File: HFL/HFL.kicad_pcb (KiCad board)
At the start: 2 copper layers, 62.6 x 37.6 mm, 26 parts, among them J1 FAULTS, J2 PWR, J3 HFR, J4 SHTDN, K1 G5V-1, K2 G5V-1, K3 G5V-1, K4 G5V-1, K5 G5V-2

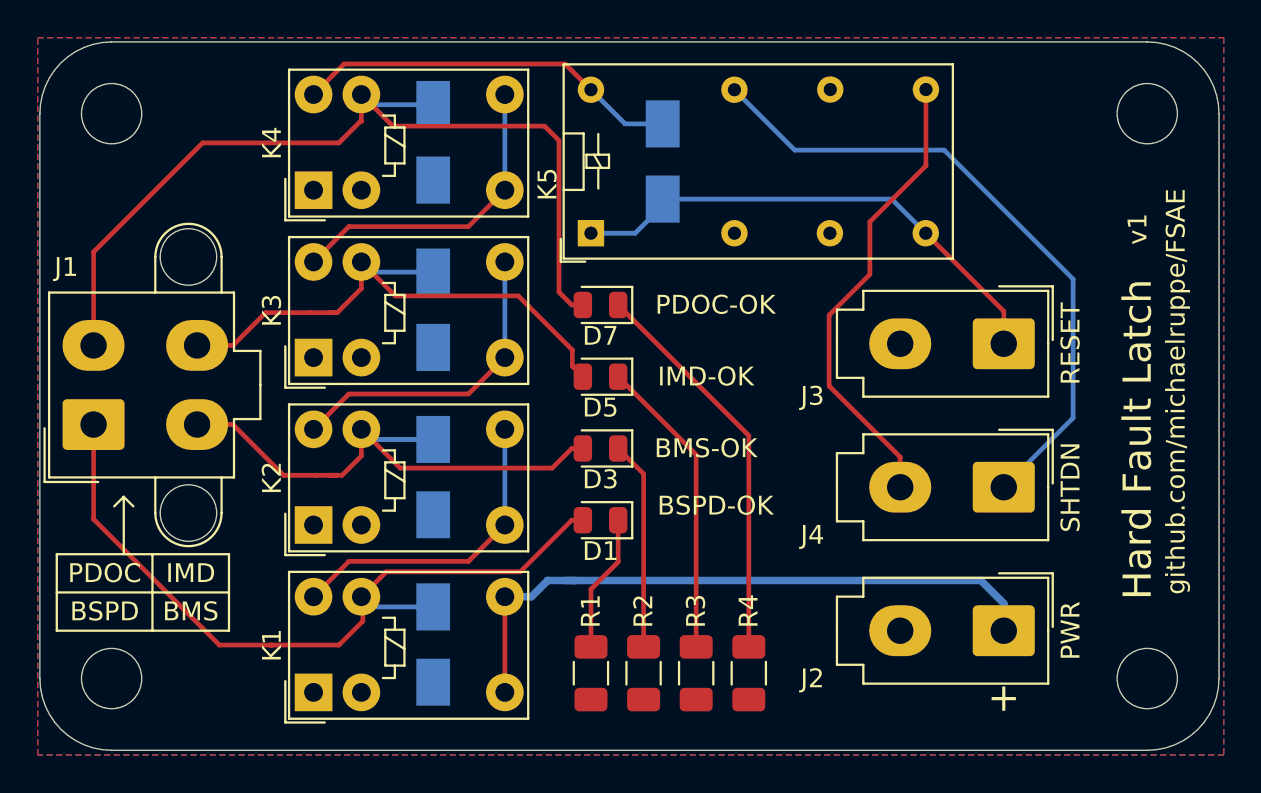
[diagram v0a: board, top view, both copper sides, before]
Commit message: Update HFL - include indicator lamp outputs (low-side)
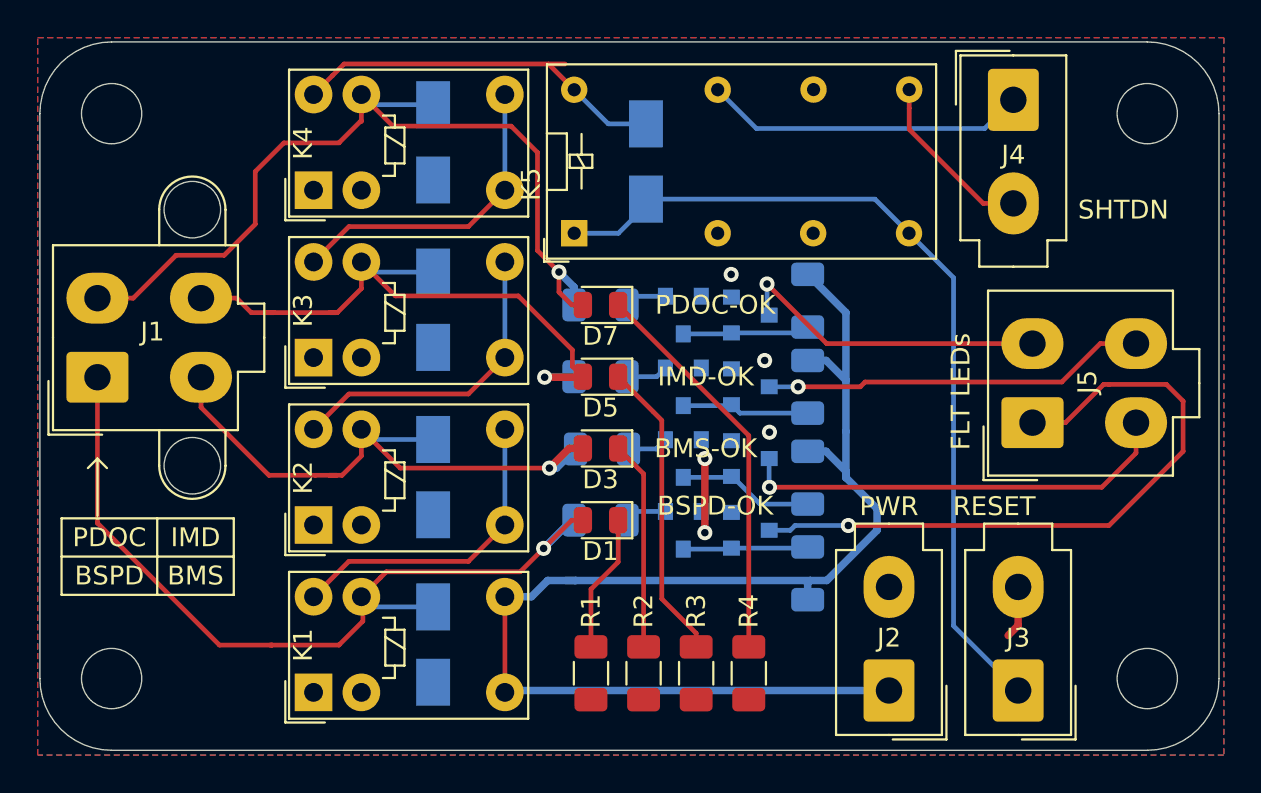
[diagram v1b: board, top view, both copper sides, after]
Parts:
- added J5: FLT-LT, Connector_Molex:Molex_Mini-Fit_Jr_5566-04A_2x02_P4.20mm_Vertical, F.Cu at (128.9, 65.9)
- added Q1: MMBT3904, Package_TO_SOT_SMD:SOT-23, B.Cu at (110.4, 67.8)
- added Q2: MMBT3904, Package_TO_SOT_SMD:SOT-23, B.Cu at (110.4, 60.2)
- added Q3: MMBT3904, Package_TO_SOT_SMD:SOT-23, B.Cu at (113.9, 67.8)
- added Q4: MMBT3904, Package_TO_SOT_SMD:SOT-23, B.Cu at (113.9, 60.2)
- added Q5: MMBT3904, Package_TO_SOT_SMD:SOT-23, B.Cu at (110.4, 64.0)
- added Q6: MMBT3904, Package_TO_SOT_SMD:SOT-23, B.Cu at (110.4, 71.7)
- added Q7: MMBT3904, Package_TO_SOT_SMD:SOT-23, B.Cu at (113.9, 64.0)
- added Q8: MMBT3904, Package_TO_SOT_SMD:SOT-23, B.Cu at (113.9, 71.7)
- added R10: 2k7, Resistor_SMD:R_1206_3216Metric, B.Cu at (106.0, 71.1)
- added R11: 2k7, Resistor_SMD:R_1206_3216Metric, B.Cu at (117.0, 64.0)
- added R12: 2k7, Resistor_SMD:R_1206_3216Metric, B.Cu at (117.0, 73.9)
- added R5: 2k7, Resistor_SMD:R_1206_3216Metric, B.Cu at (106.1, 67.3)
- added R6: 2k7, Resistor_SMD:R_1206_3216Metric, B.Cu at (106.0, 59.7)
- added R7: 2k7, Resistor_SMD:R_1206_3216Metric, B.Cu at (117.0, 68.9)
- added R8: 2k7, Resistor_SMD:R_1206_3216Metric, B.Cu at (117.0, 59.5)
- added R9: 2k7, Resistor_SMD:R_1206_3216Metric, B.Cu at (106.0, 63.5)
- moved J4 20.6 mm to (127.9, 48.8), turned to 0 degrees
- moved J3 18.4 mm to (128.2, 80.2), turned to 180 degrees
- moved J2 6.87 mm to (121.3, 80.2), turned to 180 degrees
- moved J1 2.52 mm to (79.3, 63.5)
- moved D9 0.89 mm to (108.4, 52.1)
- moved K5 0.89 mm to (104.6, 55.9)
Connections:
- net /BMS-OK renamed BMS-OK
- net /BSPD-OK renamed BSPD-OK
- net /IMD-OK renamed IMD-OK
- net /PDOC-OK renamed PDOC-OK
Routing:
- net Net-(J5-Pad1): track 0.00 -> 35.6 mm, vias 0 -> 1
- net +12V: track 34.4 -> 68.7 mm
- net Net-(J5-Pad3): track 0.00 -> 23.4 mm, vias 0 -> 1
- net Net-(J5-Pad4): track 0.00 -> 20.4 mm, vias 0 -> 1
- net /HFR1: track 27.1 -> 46.2 mm
- net Net-(J4-Pad1): track 34.7 -> 17.2 mm
- net Net-(J5-Pad2): track 0.00 -> 17.1 mm, vias 0 -> 1
- net Net-(J4-Pad2): track 24.8 -> 9.27 mm
- net Net-(Q1-Pad3): track 0.00 -> 7.23 mm
- net Net-(Q5-Pad3): track 0.00 -> 6.81 mm
- net Net-(Q2-Pad3): track 0.00 -> 6.75 mm
- net GND: track 0.00 -> 6.74 mm, vias 0 -> 5
- net Net-(Q6-Pad3): track 0.00 -> 6.65 mm
- net BSPD-OK: track 41.6 -> 46.2 mm, vias 0 -> 1
- net BMS-OK: track 29.1 -> 32.7 mm, vias 0 -> 1
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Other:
- board text added: "FLT LEDs"
- board text removed: "+"

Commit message: Finalise HFL v1
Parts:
- added J6: FOUT, Connector_Molex:Molex_Mini-Fit_Jr_5566-04A_2x02_P4.20mm_Vertical, F.Cu at (79.4, 72.0)
- J1: footprint Connector_Molex:Molex_Mini-Fit_Jr_5566-04A2_2x02_P4.20mm_Vertical -> Connector_Molex:Molex_Mini-Fit_Jr_5566-04A_2x02_P4.20mm_Vertical
- moved J1 2.54 mm to (79.4, 61.0)
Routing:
- net IMD-OK: track 34.1 -> 47.6 mm
- net PDOC-OK: track 47.1 -> 59.0 mm
- net BMS-OK: track 32.7 -> 44.3 mm
- net BSPD-OK: track 46.2 -> 52.4 mm
- net Net-(D9-Pad1): track 20.5 -> 19.6 mm
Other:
- board text removed: "BMS"
- board text removed: "BSPD"
- board text removed: "IMD"
- board text removed: "PDOC"

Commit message: Update HFL
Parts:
- removed J6: FOUT, Connector_Molex:Molex_Mini-Fit_Jr_5566-04A_2x02_P4.20mm_Vertical
- removed Q1, Q2, Q3, Q4, Q5, Q6, Q7, Q8: MMBT3904, Package_TO_SOT_SMD:SOT-23
- removed R10, R11, R12, R5, R6, R7, R8, R9: 2k7, Resistor_SMD:R_1206_3216Metric
- added G***: LOGO, HFL:logo, F.Cu at (109.0, 80.2)
- J1: value FAULTS -> Conn_01x06_Male; footprint Connector_Molex:Molex_Mini-Fit_Jr_5566-04A_2x02_P4.20mm_Vertical -> Connector_Molex:Molex_Mini-Fit_Jr_5566-06A_2x03_P4.20mm_Vertical
- J2: value PWR -> FOUT; footprint Connector_Molex:Molex_Mini-Fit_Jr_5566-02A_2x01_P4.20mm_Vertical -> Connector_Molex:Molex_Mini-Fit_Jr_5566-04A_2x02_P4.20mm_Vertical
- J3: value HFR -> PWR
- J5: value FLT-LT -> HFR; footprint Connector_Molex:Molex_Mini-Fit_Jr_5566-04A_2x02_P4.20mm_Vertical -> Connector_Molex:Molex_Mini-Fit_Jr_5566-02A_2x01_P4.20mm_Vertical
- K5: value G5V-2 -> OMRON-G2R-24; footprint Relay_THT:Relay_DPDT_Omron_G5V-2 -> HFL:OMRON-G2R-24
- R1, R2, R3, R4: moved to B.Cu
- moved J2 45.8 mm to (87.4, 49.4), turned to 0 degrees
- moved D1 27.0 mm to (79.1, 74.5), turned to 0 degrees
- moved K5 25.2 mm to (121.0, 75.0)
- moved K4 25.1 mm to (108.4, 71.4), turned to 180 degrees
- moved J1 22.0 mm to (98.1, 49.4), turned to 0 degrees
- moved D9 21.3 mm to (117.2, 71.4), turned to 180 degrees
- moved D2 20.4 mm to (81.1, 65.0), turned to 0 degrees
- moved D3 19.9 mm to (87.4, 74.5), turned to 0 degrees
- moved D8 16.5 mm to (105.9, 65.0), turned to 0 degrees
- moved R1 15.5 mm to (90.0, 79.0)
- moved R2 15.5 mm to (92.8, 79.0)
- moved R3 15.5 mm to (95.6, 79.0)
- moved R4 15.5 mm to (98.4, 79.0)
- moved D5 15.1 mm to (95.6, 74.5), turned to 0 degrees
- moved D7 14.9 mm to (103.9, 74.5), turned to 0 degrees
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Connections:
- J2 pad 1: +12V -> BSPD-OK
- J2 pad 2: GND -> PDOC-OK
- J3 pad 1: /HFR1 -> +12V
- J5 pad 1: Net-(J5-Pad1) -> /HFR1
- J5 pad 2: Net-(J5-Pad2) -> GND
- K1 pad 5: +12V -> Net-(J1-Pad5)
- K1 pad 6: +12V -> Net-(J1-Pad5)
- K5 pad 4: GND -> Net-(J4-Pad2)
- K5 pad 6: Net-(K5-Pad6) -> GND
- K5 pad 8: /HFR1 -> Net-(D9-Pad1)
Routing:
- net Net-(J5-Pad1): track 35.6 -> 0.00 mm, vias 1 -> 0
- net +12V: track 68.7 -> 39.6 mm
- net Net-(J1-Pad5): track 0.00 -> 27.4 mm
- net Net-(J5-Pad3): track 23.4 -> 0.00 mm, vias 1 -> 0
- net Net-(J5-Pad4): track 20.4 -> 0.00 mm, vias 1 -> 0
- net IMD-OK: track 47.6 -> 28.8 mm
- net Net-(J4-Pad2): track 9.27 -> 27.0 mm
- net Net-(J5-Pad2): track 17.1 -> 0.00 mm, vias 1 -> 0
- net Net-(D7-Pad1): track 21.0 -> 6.05 mm, vias 0 -> 1
- net PDOC-OK: track 59.0 -> 44.2 mm, vias 1 -> 0
- net Net-(D5-Pad1): track 16.1 -> 4.36 mm, vias 0 -> 1
- net BSPD-OK: track 52.4 -> 42.7 mm
- net Net-(J4-Pad1): track 17.2 -> 25.3 mm
- net Net-(Q1-Pad3): track 7.23 -> 0.00 mm
- net Net-(D1-Pad1): track 7.33 -> 14.4 mm, vias 0 -> 1
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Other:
- board text added: "BMS"
- board text added: "BSPD"
- board text added: "HFR"
- board text added: "IMD"
- board text added: "PDOC"
- board text removed: "BMS-OK"
- board text removed: "BSPD-OK"
- board text removed: "FLT LEDs"
- board text removed: "IMD-OK"
- board text removed: "PDOC-OK"
- board text removed: "RESET"

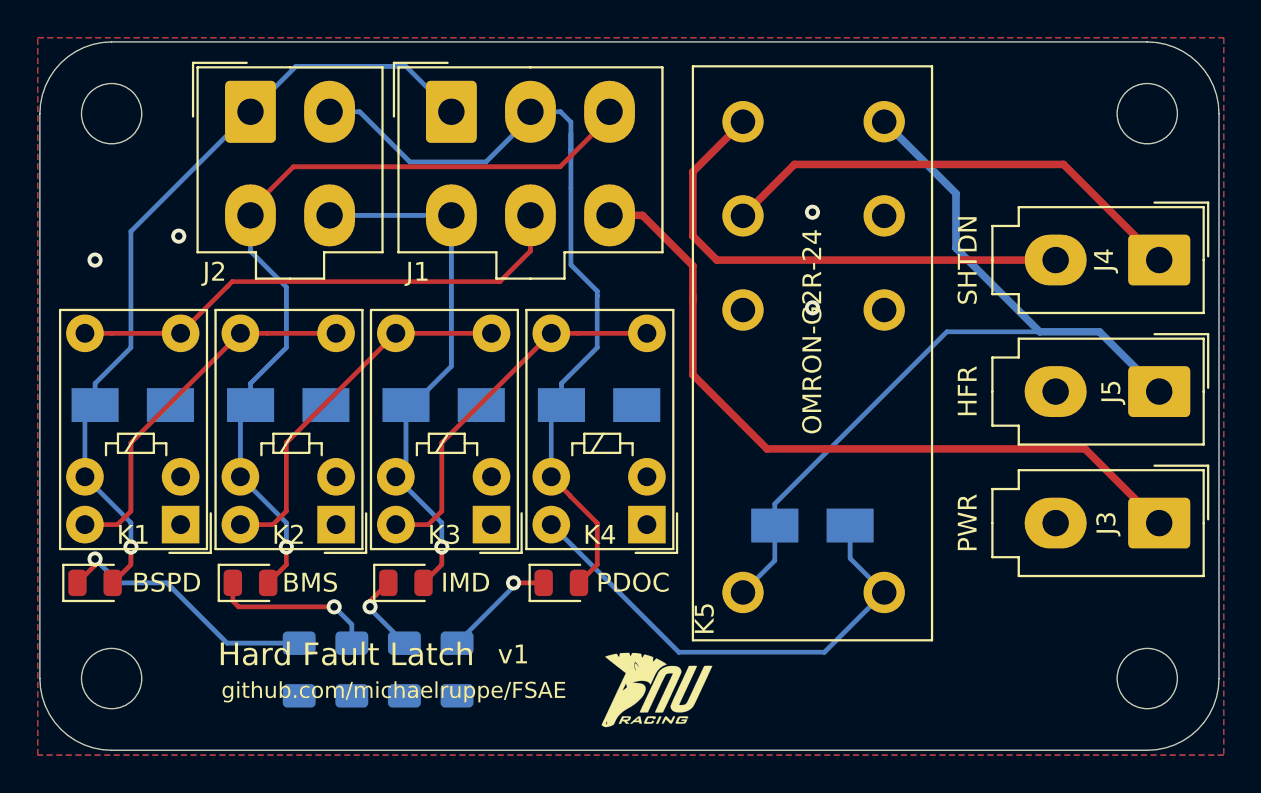
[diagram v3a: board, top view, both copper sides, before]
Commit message: update j2 pinout to match CCU board
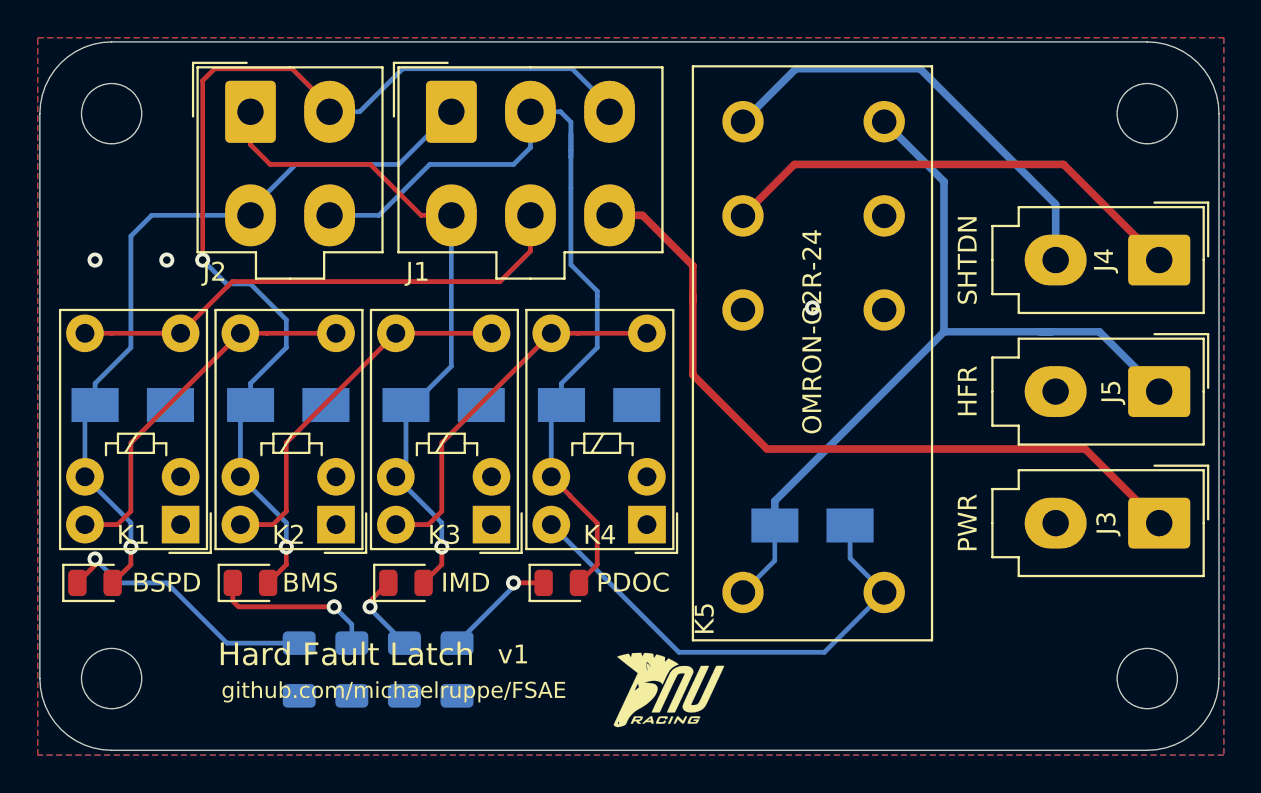
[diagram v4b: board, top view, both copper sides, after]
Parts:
- moved G*** 0.64 mm to (109.6, 80.2)
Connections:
- net Net-(J1-Pad5) renamed /BOTS-OK
- J2 pad 1: BSPD-OK -> IMD-OK
- J2 pad 2: PDOC-OK -> BMS-OK
- J2 pad 3: BMS-OK -> BSPD-OK
- J2 pad 4: IMD-OK -> PDOC-OK
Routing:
- net BMS-OK: track 44.4 -> 57.0 mm, vias 1 -> 2
- net IMD-OK: track 28.8 -> 36.3 mm
- net Net-(J4-Pad2): track 27.0 -> 23.7 mm
- net BSPD-OK: track 42.7 -> 41.1 mm
- net /HFR1: track 45.5 -> 44.1 mm
- net PDOC-OK: track 44.2 -> 45.5 mm
- net GND: vias 4 -> 3
